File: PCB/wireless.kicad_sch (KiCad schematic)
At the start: 8 parts

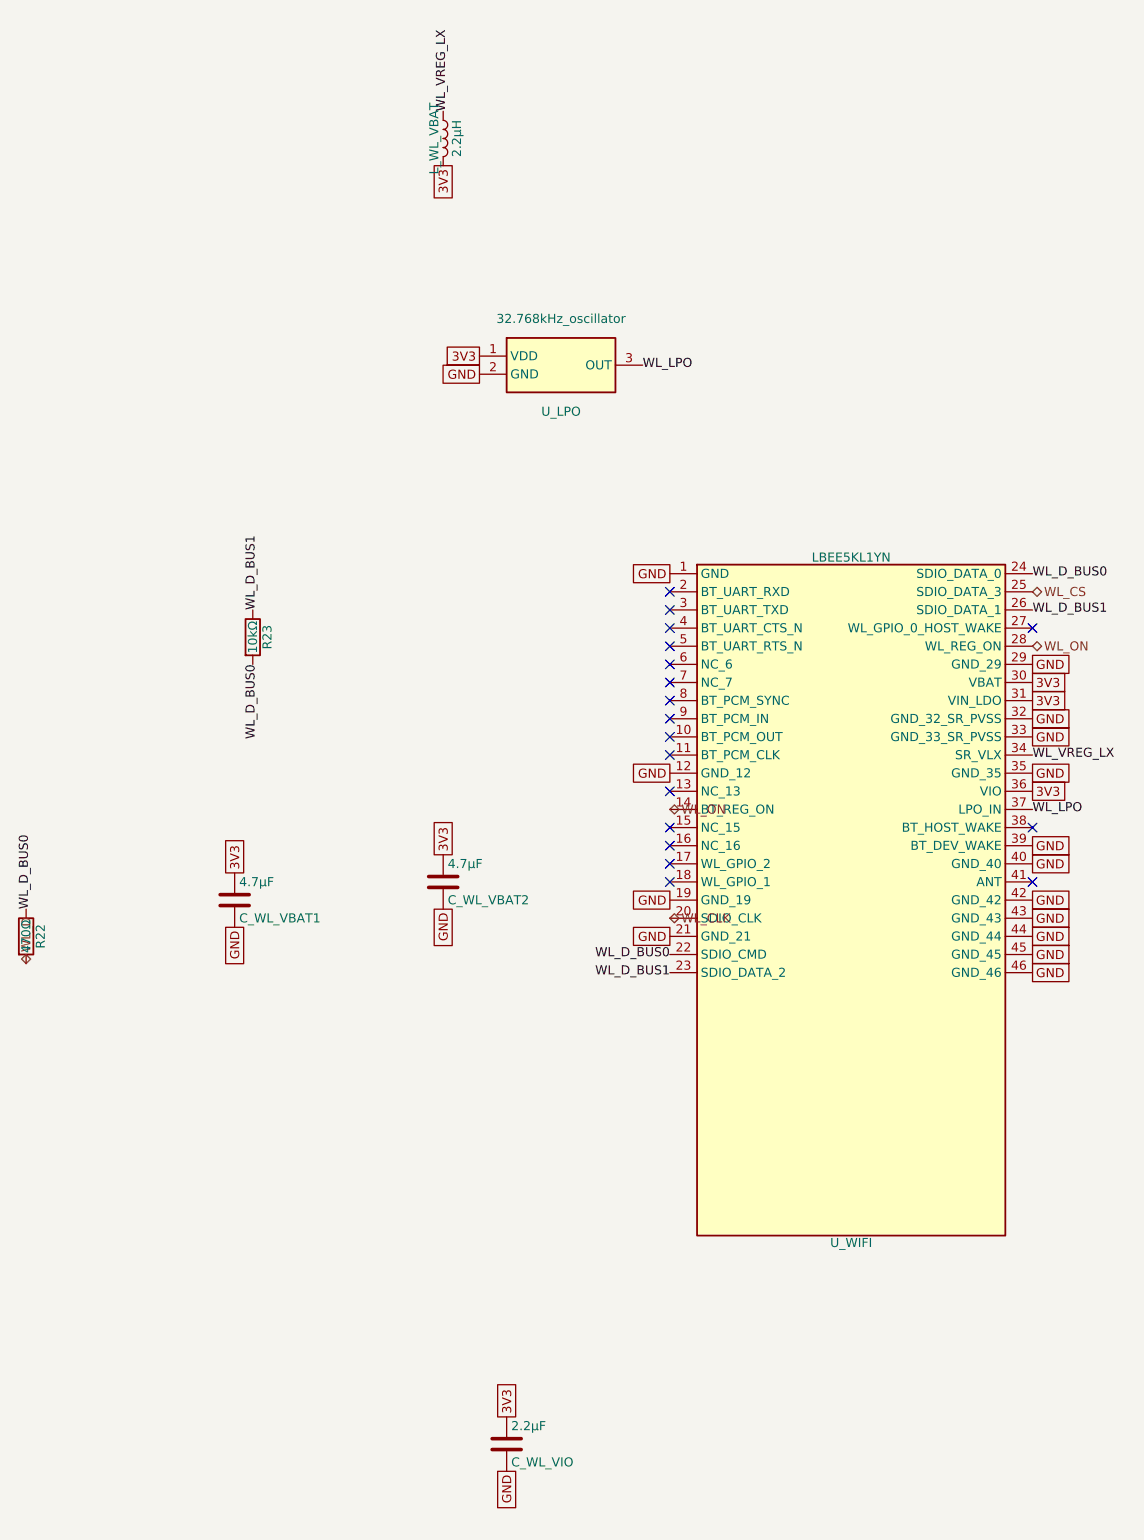
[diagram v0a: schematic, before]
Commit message: refactor: erc is clean
This gets the schematic as clean as it can be.
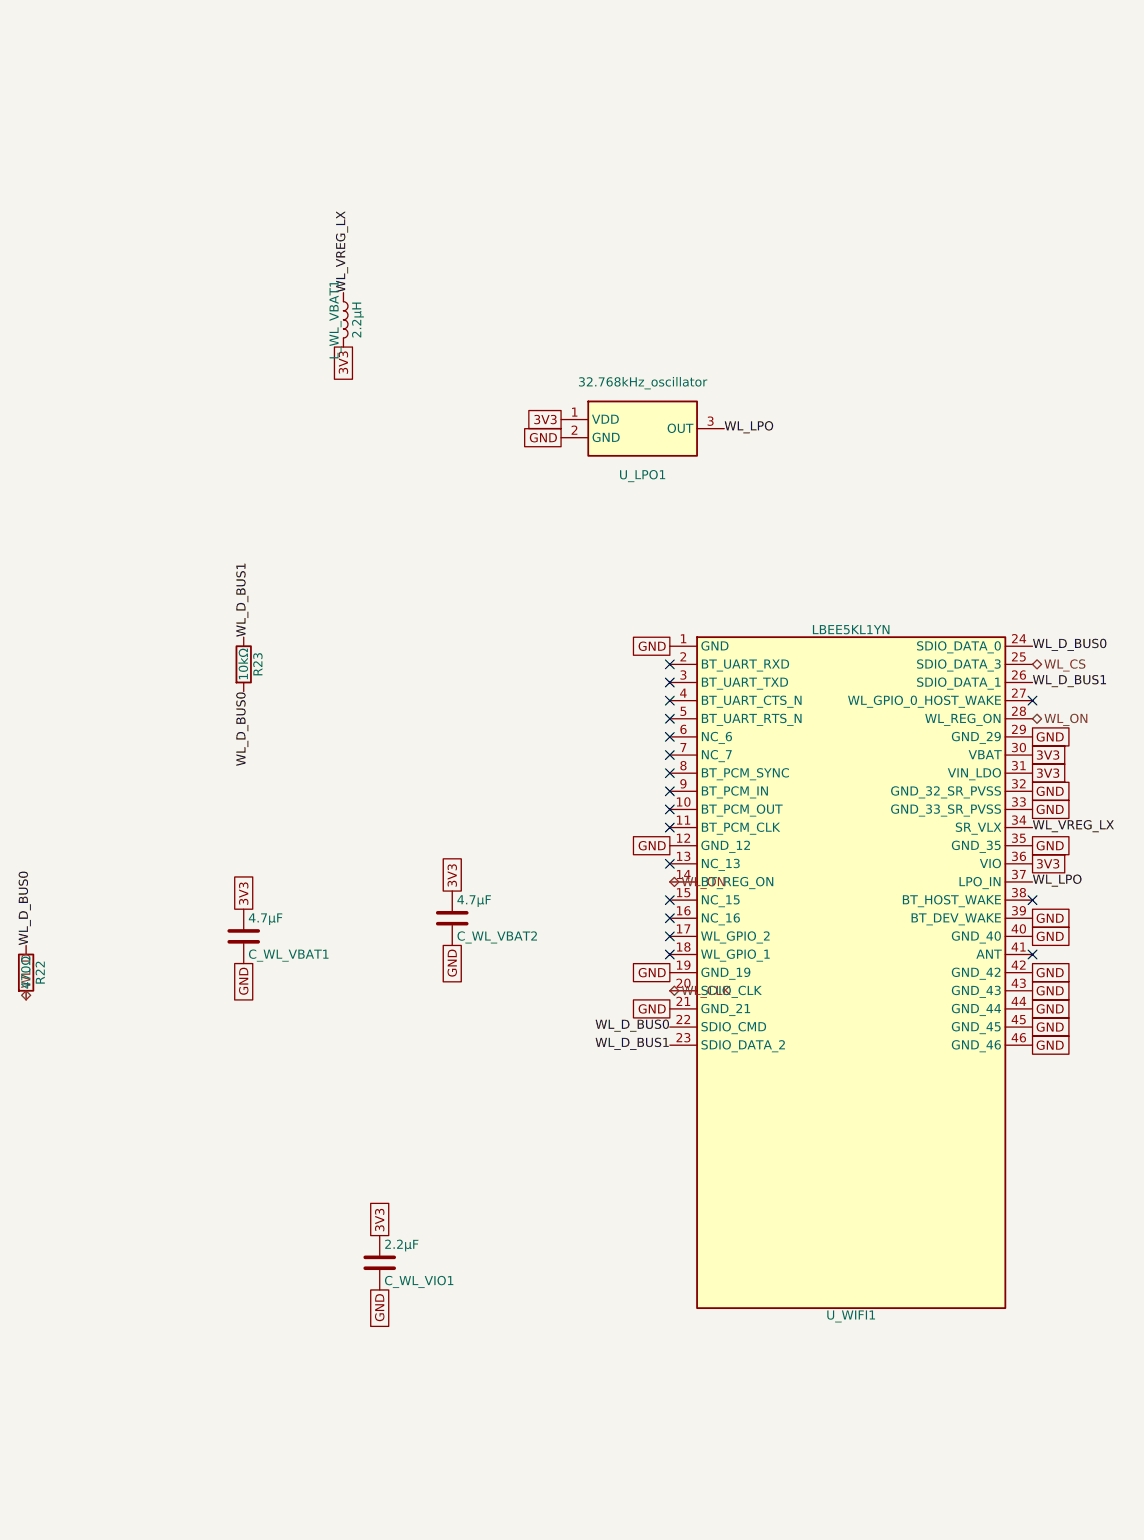
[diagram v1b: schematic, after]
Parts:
- removed C_WL_VIO: 2.2µF, symbol Device:C
- removed L_WL_VBAT: 2.2µH, symbol Device:L
- removed U_LPO: 32.768kHz_oscillator, symbol SnipsControllers:Osc_32k768_3pin
- removed U_WIFI: LBEE5KL1YN, symbol SnipsControllers:Murata_Type1YN
- added C_WL_VIO1: 2.2µF, symbol Device:C
- added L_WL_VBAT1: 2.2µH, symbol Device:L
- added U_LPO1: 32.768kHz_oscillator, symbol SnipsControllers:Osc_32k768_3pin
- added U_WIFI1: LBEE5KL1YN, symbol SnipsControllers:Murata_Type1YN
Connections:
- net 3V3: now also C_WL_VIO1.1, L_WL_VBAT1.2, U_LPO1.1 (VDD), U_WIFI1.30 (VBAT), U_WIFI1.31 (VIN_LDO), U_WIFI1.36 (VIO)
- net GND: now also C_WL_VIO1.2, U_LPO1.2 (GND), U_WIFI1.1 (GND), U_WIFI1.12 (GND_12), U_WIFI1.19 (GND_19), U_WIFI1.21 (GND_21), U_WIFI1.29 (GND_29), U_WIFI1.32 (GND_32_SR_PVSS), U_WIFI1.33 (GND_33_SR_PVSS), U_WIFI1.35 (GND_35), U_WIFI1.39 (BT_DEV_WAKE), U_WIFI1.40 (GND_40), U_WIFI1.42 (GND_42), U_WIFI1.43 (GND_43), U_WIFI1.44 (GND_44), U_WIFI1.45 (GND_45), U_WIFI1.46 (GND_46)
- net WL_CLK: now also U_WIFI1.20 (SDIO_CLK)
- net WL_CS: now also U_WIFI1.25 (SDIO_DATA_3)
- net WL_D_BUS0: now also U_WIFI1.22 (SDIO_CMD), U_WIFI1.24 (SDIO_DATA_0)
- net WL_D_BUS1: now also U_WIFI1.23 (SDIO_DATA_2), U_WIFI1.26 (SDIO_DATA_1)
- net WL_LPO: now also U_LPO1.3 (OUT), U_WIFI1.37 (LPO_IN)
- net WL_ON: now also U_WIFI1.14 (BT_REG_ON), U_WIFI1.28 (WL_REG_ON)
- net WL_VREG_LX: now also L_WL_VBAT1.1, U_WIFI1.34 (SR_VLX)
